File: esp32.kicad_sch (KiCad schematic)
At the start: 15 parts, among them J1 DIN-5_180degree, J2 DIN-5_180degree, U1 ESP32-S3-DevKitC, U3 6N138, U4 6N138, U6 LM66100DCK

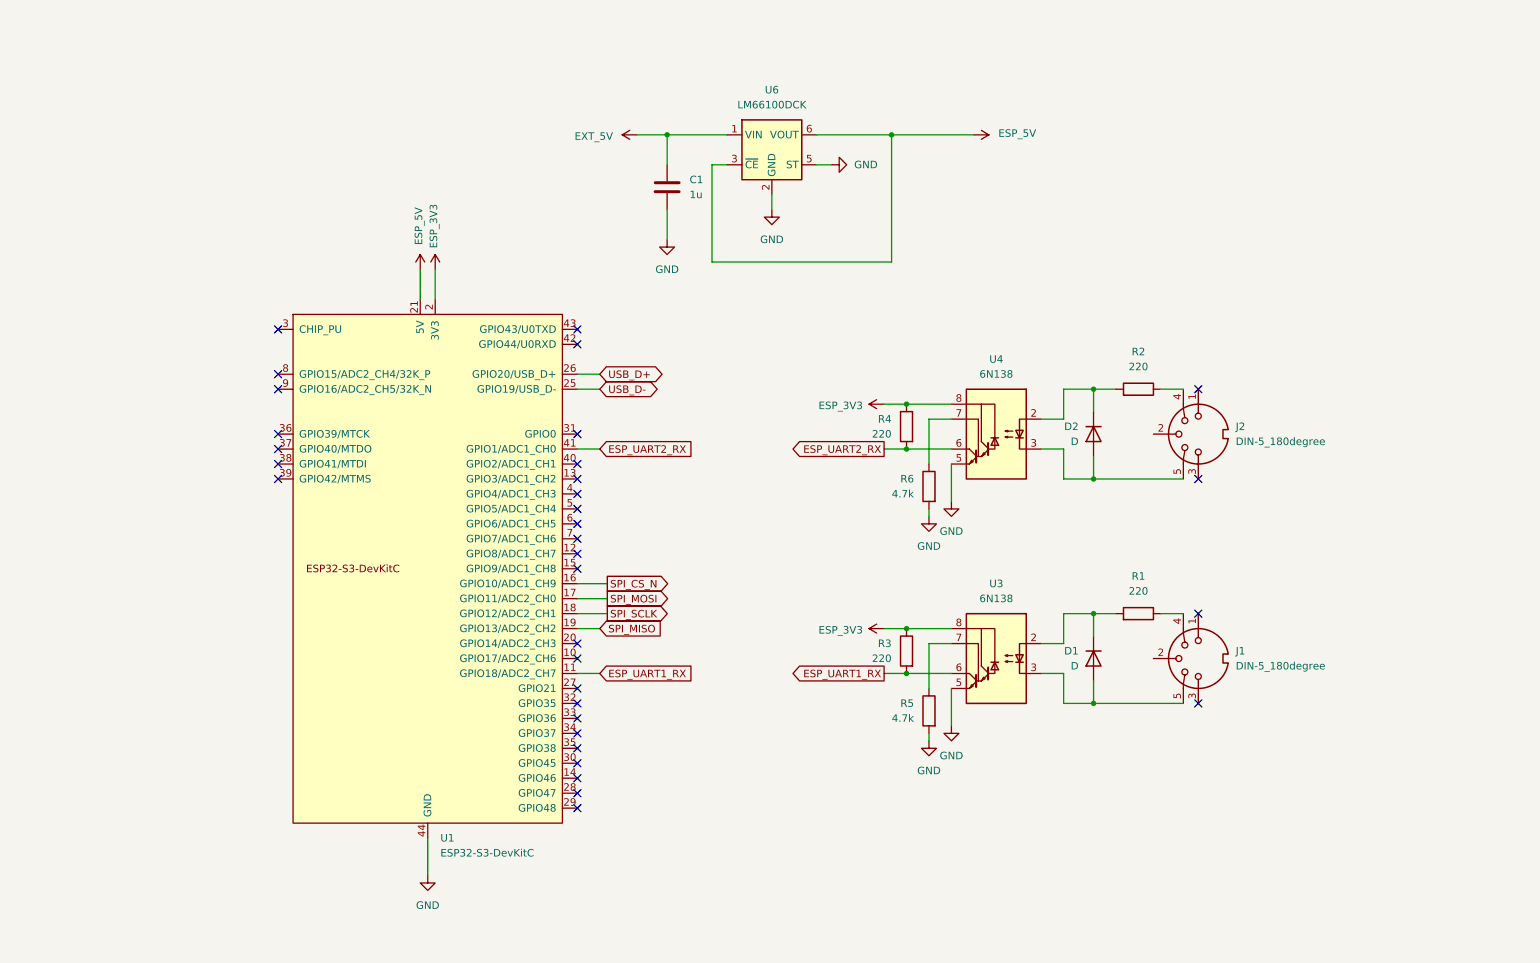
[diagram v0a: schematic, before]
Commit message: Added pin headers for SPI3, I2C0 and I2C1
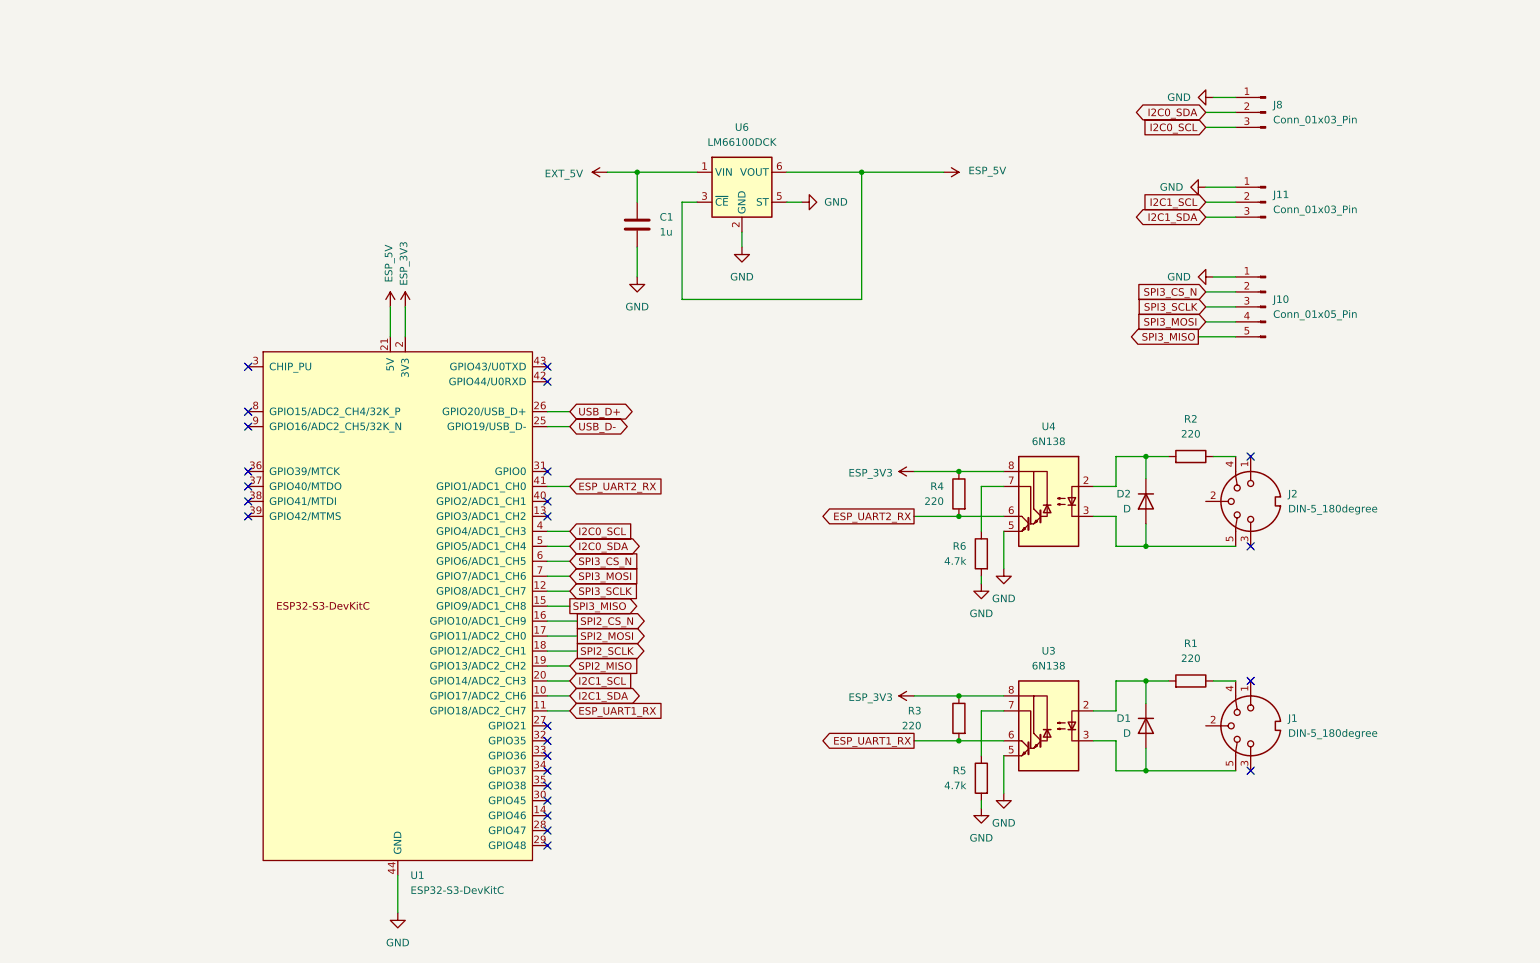
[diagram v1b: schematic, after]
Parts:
- added J10: Conn_01x05_Pin, symbol Connector:Conn_01x05_Pin
- added J11, J8: Conn_01x03_Pin, symbol Connector:Conn_01x03_Pin
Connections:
- net GND: now also J10.1 (Pin_1), J11.1 (Pin_1), J8.1 (Pin_1)
- net I2C1_SDA: now reaches U1.10 (GPIO17/ADC2_CH6)
- net I2C1_SDA: now also J11.3 (Pin_3)
- net SPI3_SCLK: now reaches U1.12 (GPIO8/ADC1_CH7)
- net SPI3_SCLK: now also J10.3 (Pin_3)
- net SPI3_MISO: now reaches U1.15 (GPIO9/ADC1_CH8)
- net SPI3_MISO: now also J10.5 (Pin_5)
- net I2C1_SCL: now reaches U1.20 (GPIO14/ADC2_CH3)
- net I2C1_SCL: now also J11.2 (Pin_2)
- net I2C0_SCL: now reaches U1.4 (GPIO4/ADC1_CH3)
- net I2C0_SCL: now also J8.3 (Pin_3)
- net I2C0_SDA: now reaches U1.5 (GPIO5/ADC1_CH4)
- net I2C0_SDA: now also J8.2 (Pin_2)
- net SPI3_CS_N: now reaches U1.6 (GPIO6/ADC1_CH5)
- net SPI3_CS_N: now also J10.2 (Pin_2)
- net SPI3_MOSI: now reaches U1.7 (GPIO7/ADC1_CH6)
- net SPI3_MOSI: now also J10.4 (Pin_4)
- net SPI_CS_N renamed SPI2_CS_N
- net SPI_MISO renamed SPI2_MISO
- net SPI_MOSI renamed SPI2_MOSI
- net SPI_SCLK renamed SPI2_SCLK
- no-connect marks 33 -> 25
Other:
- moved on the sheet: C1, D1, D2, J1, J2, R1, R2, R3, R4, R5, R6, U1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

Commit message: Added I2C pull-ups
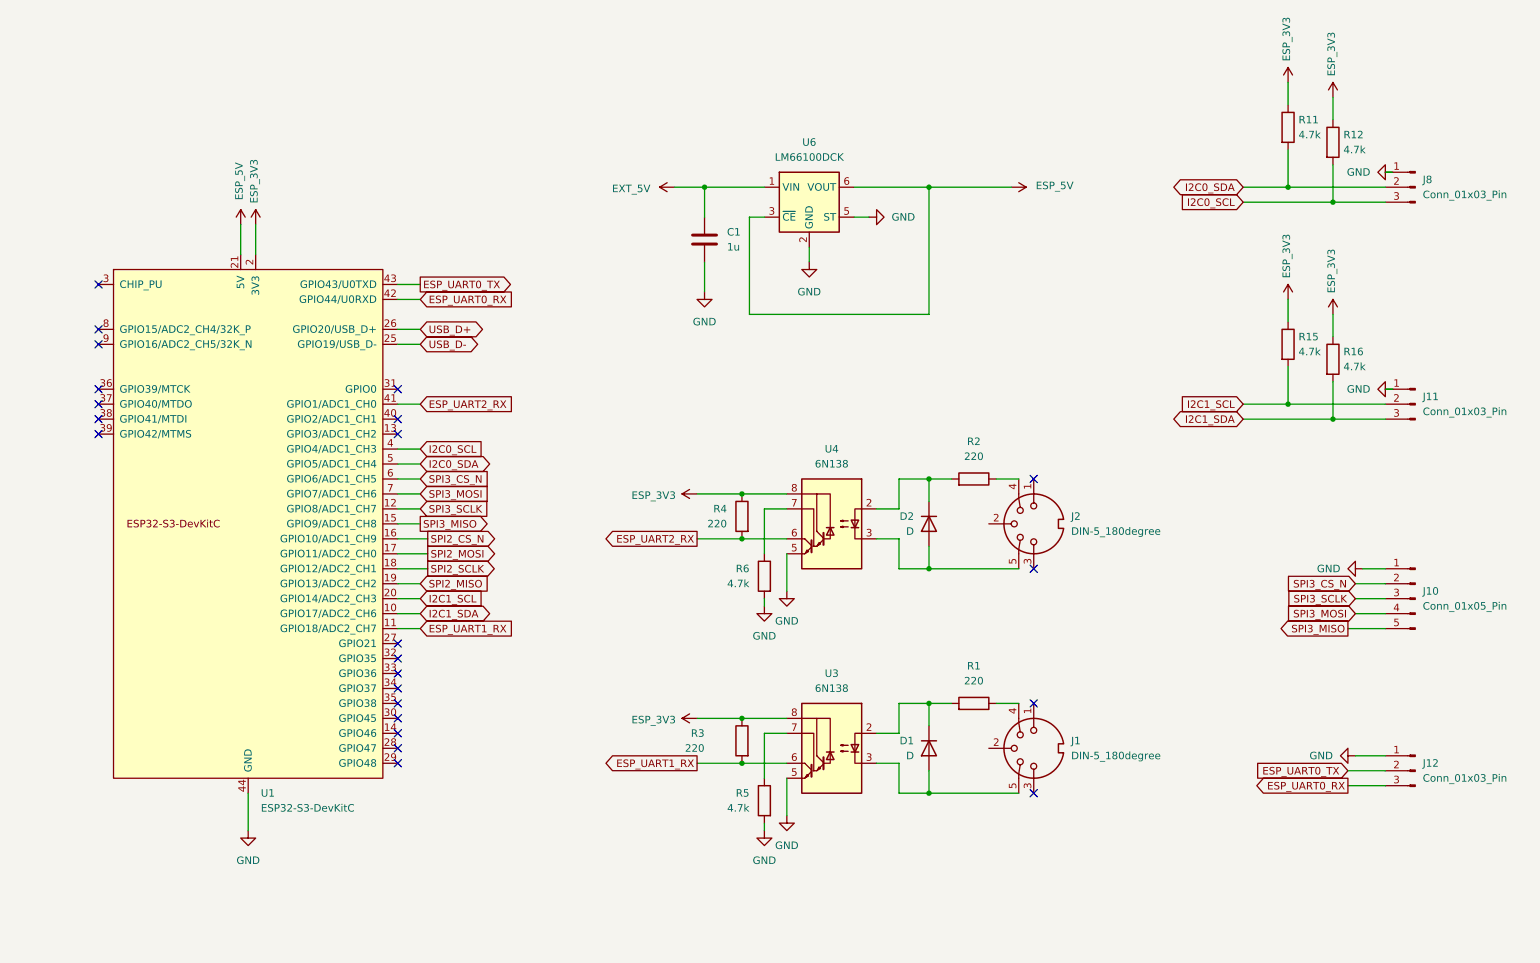
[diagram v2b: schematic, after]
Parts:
- added J12: Conn_01x03_Pin, symbol Connector:Conn_01x03_Pin
- added R11, R12, R15, R16: 4.7k, symbol Device:R
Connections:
- net ESP_3V3: now also R11.1, R12.1, R15.1, R16.1
- net GND: now also J12.1 (Pin_1)
- net I2C0_SCL: now also R12.2
- net I2C0_SDA: now also R11.2
- net I2C1_SCL: now also R15.2
- net I2C1_SDA: now also R16.2
- net ESP_UART0_RX: now reaches U1.42 (GPIO44/U0RXD)
- net ESP_UART0_RX: now also J12.3 (Pin_3)
- net ESP_UART0_TX: now reaches U1.43 (GPIO43/U0TXD)
- net ESP_UART0_TX: now also J12.2 (Pin_2)
- no-connect marks 25 -> 23
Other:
- moved on the sheet: C1, D1, D2, J1, J10, J11, J2, J8, R1, R2, R3, R4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

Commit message: Moved UART0 header to new ESP32-S3 pins.
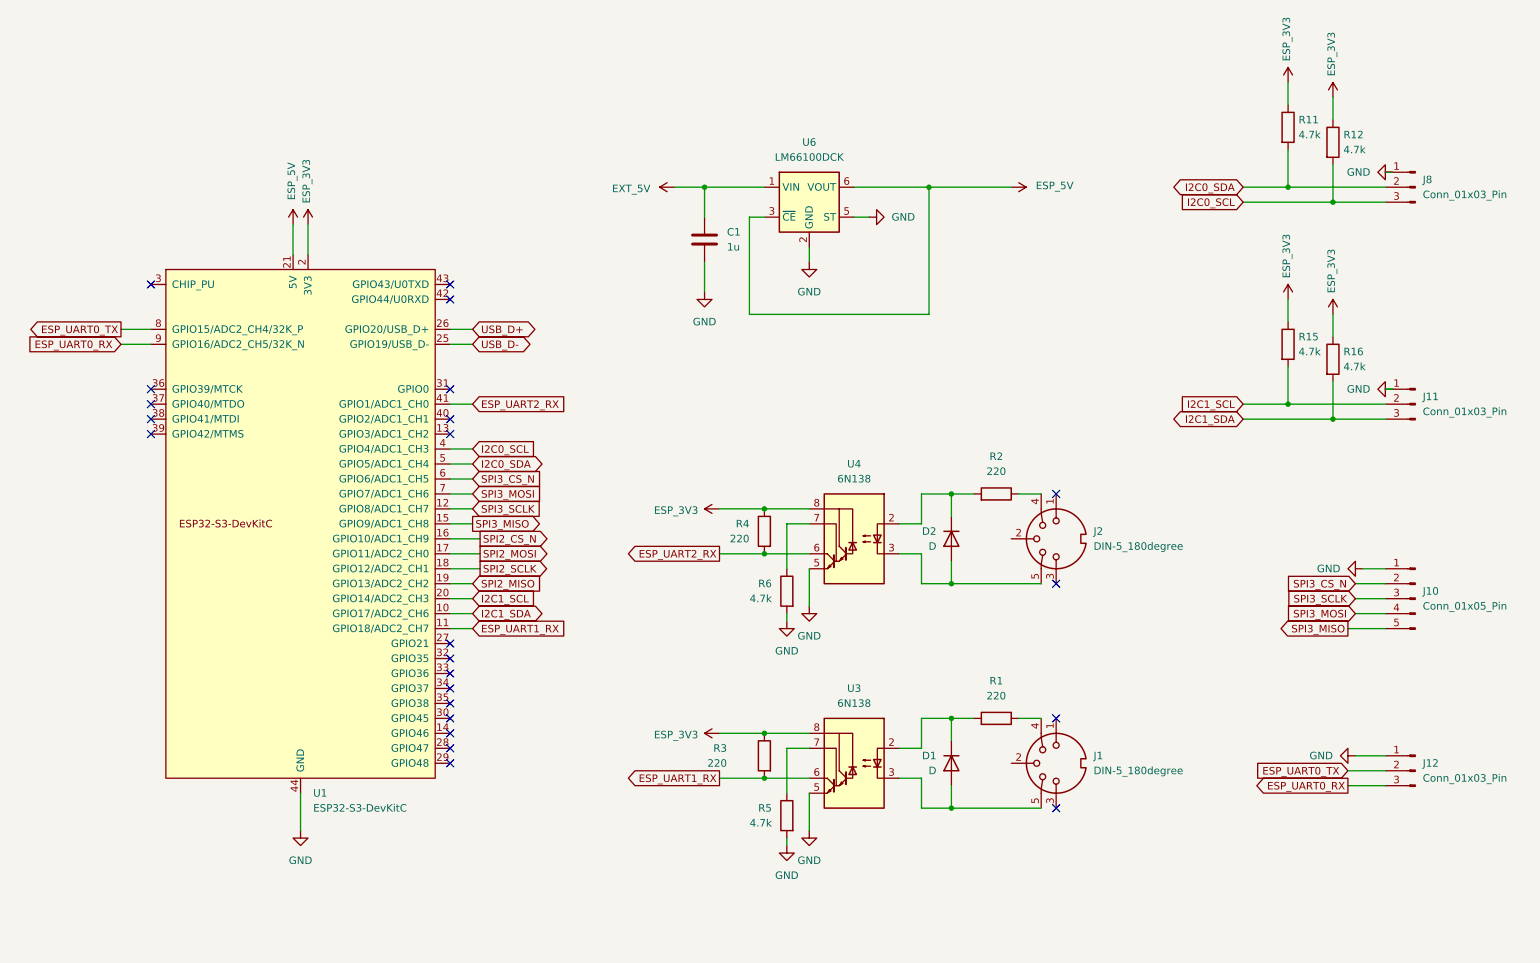
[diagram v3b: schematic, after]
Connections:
- net ESP_UART0_RX: now also U1.9 (GPIO16/ADC2_CH5/32K_N); no longer U1.42 (GPIO44/U0RXD)
- net ESP_UART0_TX: now also U1.8 (GPIO15/ADC2_CH4/32K_P); no longer U1.43 (GPIO43/U0TXD)
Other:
- moved on the sheet: D1, D2, J1, J2, R1, R2, R3, R4, R5, R6, U1, U3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

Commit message: Correcting ERC errors
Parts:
- U1: symbol PCM_Espressif:ESP32-S3-DevKitC -> noaidi-fpga-synth:ESP32-S3-DevKitC
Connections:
- no-connect marks 23 -> 25
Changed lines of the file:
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@@
 	)
 	(no_connect
+		(at 184.15 147.32)
+	)
+	(no_connect
 		(at 88.9 134.62)
 	)
@@
 	)
 	(no_connect
+		(at 184.15 109.22)
+	)
+	(no_connect
 		(at 88.9 132.08)
 	)
@@
 	)
 	(symbol
+		(lib_id "power:GND")
+		(at 146.05 161.29 0)
+		(mirror y)
+		(unit 1)
+		(body_style 1)
+		(exclude_from_sim no)
+		(in_bom yes)
+		(on_board yes)
+		(in_pos_files yes)
+		(dnp no)
+		(fields_autoplaced yes)
+		(property "Reference" "#PWR058"
+			(at 146.05 167.64 0)
+			(hide yes)
+			(show_name no)
+			(do_not_autoplace no)
+			(effects
+				(font
+					(size 1.27 1.27)
+				)
+			)
+		)
+		(property "Value" "GND"
+			(at 146.05 166.37 0)
+			(show_name no)
+			(do_not_autoplace no)
+			(effects
+				(font
+					(size 1.27 1.27)
+				)
+			)
+		)
+		(property "Footprint" ""
+			(at 146.05 161.29 0)
+			(hide yes)
+			(show_name no)
+			(do_not_autoplace no)
+			(effects
+				(font
+					(size 1.27 1.27)
+				)
+			)
+		)
+		(property "Datasheet" ""
+			(at 146.05 161.29 0)
+			(hide yes)
+			(show_name no)
+			(do_not_autoplace no)
+			(effects
+				(font
+					(size 1.27 1.27)
+				)
+			)
+		)
+		(property "Description" "Power symbol creates a global label with name \"GND\" , ground"
+			(at 146.05 161.29 0)
+			(hide yes)
+			(show_name no)
+			(do_not_autoplace no)
+			(effects
+				(font
+					(size 1.27 1.27)
+				)
+			)
+		)
+		(pin "1"
+		)
+		(instances
+			(project "noaidi-fpga-synth"
+				(path "/2d9f22c5-89d1-4483-a813-1bb0a493733a"
+					(reference "#PWR058")
+					(unit 1)
+				)
+			)
+		)
+	)
+	(symbol
 		(lib_id "power:+3V3")
 		(at 134.62 142.24 90)
@@
 	(symbol
 		(lib_id "power:GND")
-		(at 146.05 123.19 0)
-		(mirror y)
-		(unit 1)
-		(body_style 1)
-		(exclude_from_sim no)
-		(in_bom yes)
-		(on_board yes)
-		(in_pos_files yes)
-		(dnp no)
-		(fields_autoplaced yes)
-		(property "Reference" "#PWR06"
-			(at 146.05 129.54 0)
-			(hide yes)
-			(show_name no)
-			(do_not_autoplace no)
-			(effects
-				(font
-					(size 1.27 1.27)
-				)
-			)
-		)
-		(property "Value" "GND"
-			(at 146.05 128.27 0)
-			(show_name no)
-			(do_not_autoplace no)
-			(effects
-				(font
-					(size 1.27 1.27)
-				)
-			)
-		)
-		(property "Footprint" ""
-			(at 146.05 123.19 0)
-			(hide yes)
-			(show_name no)
-			(do_not_autoplace no)
-			(effects
-				(font
-					(size 1.27 1.27)
-				)
-			)
-		)
-		(property "Datasheet" ""
-			(at 146.05 123.19 0)
-			(hide yes)
-			(show_name no)
-			(do_not_autoplace no)
-			(effects
-				(font
-					(size 1.27 1.27)
-				)
-			)
-		)
-		(property "Description" "Power symbol creates a global label with name \"GND\" , ground"
-			(at 146.05 123.19 0)
-			(hide yes)
-			(show_name no)
-			(do_not_autoplace no)
-			(effects
-				(font
-					(size 1.27 1.27)
-				)
-			)
-		)
-		(pin "1"
-		)
-		(instances
-			(project "noaidi-fpga-synth"
-				(path "/2d9f22c5-89d1-4483-a813-1bb0a493733a"
-					(reference "#PWR06")
-					(unit 1)
-				)
-			)
-		)
-	)
-	(symbol
-		(lib_id "power:GND")
 		(at 63.5 158.75 0)
 		(unit 1)
@@
 	)
 	(symbol
-		(lib_id "power:GND")
-		(at 146.05 161.29 0)
-		(mirror y)
-		(unit 1)
-		(body_style 1)
-		(exclude_from_sim no)
-		(in_bom yes)
-		(on_board yes)
-		(in_pos_files yes)
-		(dnp no)
-		(fields_autoplaced yes)
-		(property "Reference" "#PWR05"
-			(at 146.05 167.64 0)
-			(hide yes)
-			(show_name no)
-			(do_not_autoplace no)
-			(effects
-				(font
-					(size 1.27 1.27)
-				)
-			)
-		)
-		(property "Value" "GND"
-			(at 146.05 166.37 0)
-			(show_name no)
-			(do_not_autoplace no)
-			(effects
-				(font
-					(size 1.27 1.27)
-				)
-			)
-		)
-		(property "Footprint" ""
-			(at 146.05 161.29 0)
-			(hide yes)
-			(show_name no)
-			(do_not_autoplace no)
-			(effects
-				(font
-					(size 1.27 1.27)
-				)
-			)
-		)
-		(property "Datasheet" ""
-			(at 146.05 161.29 0)
-			(hide yes)
-			(show_name no)
-			(do_not_autoplace no)
-			(effects
-				(font
-					(size 1.27 1.27)
-				)
-			)
-		)
-		(property "Description" "Power symbol creates a global label with name \"GND\" , ground"
-			(at 146.05 161.29 0)
-			(hide yes)
-			(show_name no)
-			(do_not_autoplace no)
-			(effects
-				(font
-					(size 1.27 1.27)
-				)
-			)
-		)
-		(pin "1"
-		)
-		(instances
-			(project "noaidi-fpga-synth"
-				(path "/2d9f22c5-89d1-4483-a813-1bb0a493733a"
-					(reference "#PWR05")
-					(unit 1)
-				)
-			)
-		)
-	)
-	(symbol
 		(lib_id "Connector:Conn_01x03_Pin")
 		(at 252.73 148.59 0)
@@
 	)
 	(symbol
-		(lib_id "PCM_Espressif:ESP32-S3-DevKitC")
+		(lib_id "noaidi-fpga-synth:ESP32-S3-DevKitC")
 		(at 63.5 106.68 0)
 		(unit 1)
@@
 					(unit 1)
 				)
+			)
+		)
+	)
+	(symbol
+		(lib_id "power:GND")
+		(at 146.05 123.19 0)
+		(mirror y)
+		(unit 1)
+		(body_style 1)
+		(exclude_from_sim no)
+		(in_bom yes)
+		(on_board yes)
+		(in_pos_files yes)
+		(dnp no)
+		(fields_autoplaced yes)
+		(property "Reference" "#PWR059"
+			(at 146.05 129.54 0)
+			(hide yes)
+			(show_name no)
+			(do_not_autoplace no)
+			(effects
+				(font
+					(size 1.27 1.27)
+				)
+			)
+		)
+		(property "Value" "GND"
+			(at 146.05 128.27 0)
+			(show_name no)
+			(do_not_autoplace no)
+			(effects
+				(font
+					(size 1.27 1.27)
+				)
+			)
+		)
+		(property "Footprint" ""
+			(at 146.05 123.19 0)
+			(hide yes)
+			(show_name no)
+			(do_not_autoplace no)
+			(effects
+				(font
+					(size 1.27 1.27)
+				)
+			)
+		)
+		(property "Datasheet" ""
+			(at 146.05 123.19 0)
+			(hide yes)
+			(show_name no)
+			(do_not_autoplace no)
+			(effects
+				(font
+					(size 1.27 1.27)
+				)
+			)
+		)
+		(property "Description" "Power symbol creates a global label with name \"GND\" , ground"
+			(at 146.05 123.19 0)
+			(hide yes)
+			(show_name no)
+			(do_not_autoplace no)
+			(effects
+				(font
+					(size 1.27 1.27)
+				)
+			)
+		)
+		(pin "1"
+		)
+		(instances
+			(project "noaidi-fpga-synth"
+				(path "/2d9f22c5-89d1-4483-a813-1bb0a493733a"
+					(reference "#PWR059")
+					(unit 1)
+				)
